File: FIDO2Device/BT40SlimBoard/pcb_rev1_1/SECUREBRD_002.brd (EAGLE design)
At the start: 30 x 30 mm, 36 parts, among them CN1 USB4105-GF-A, CN3 IF_6PIN, SW1 SKRPACE010, SW2 SKTADAE010, U1 BT40, U2 ADP122ACPZ-3.3-R7, U3 RV-3028-C7

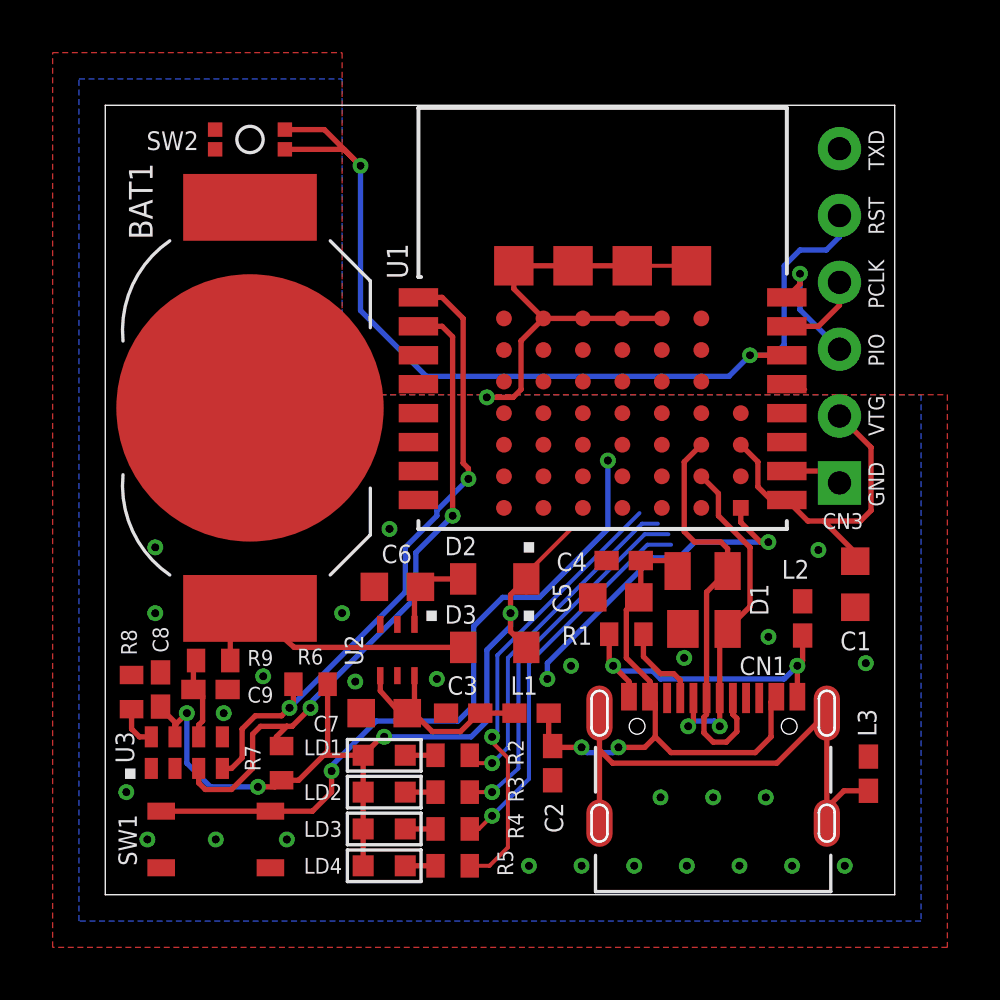
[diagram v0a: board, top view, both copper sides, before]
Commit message: 配線レイアウトを修正
・基板右側の配線レイアウトを変更
（配線が基板の端を通らないよう修正）
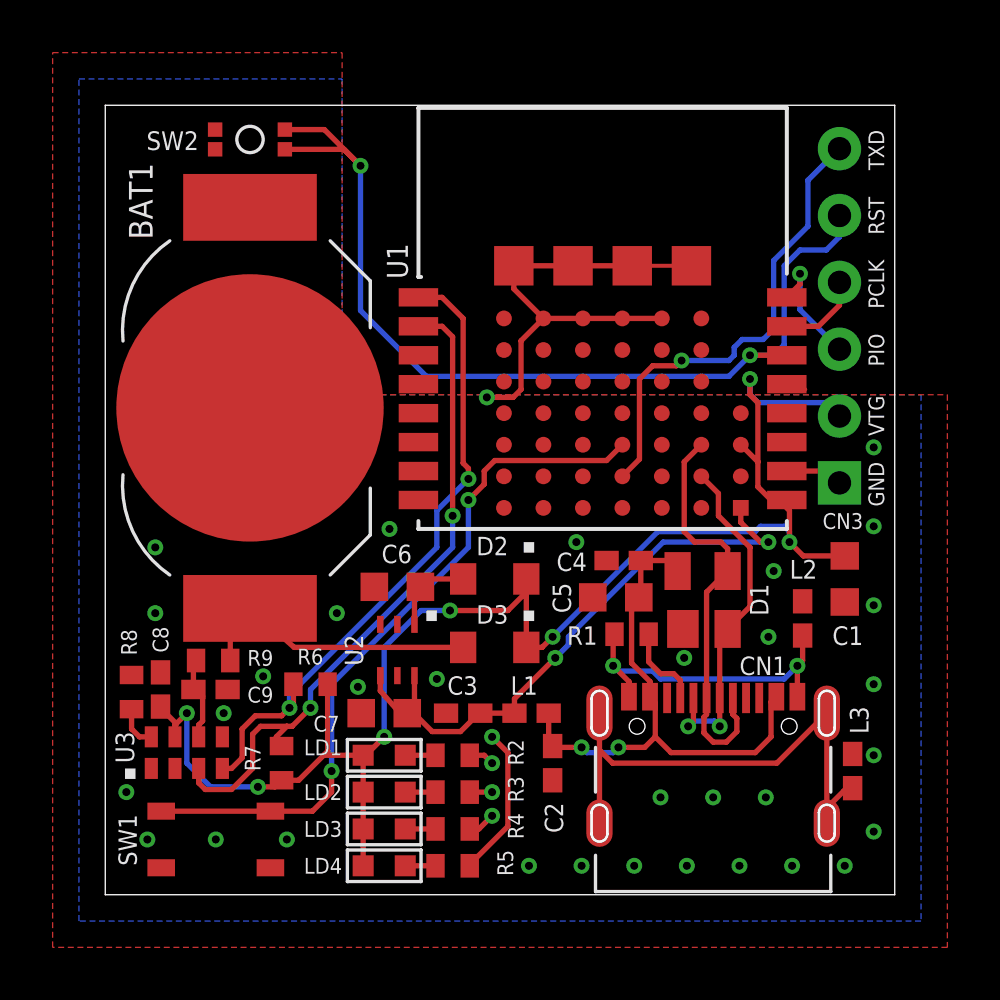
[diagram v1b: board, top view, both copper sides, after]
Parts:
- moved L3 0.61 mm to (28.4, 4.70)
- moved C1 0.45 mm to (28.1, 12.0)
- moved R1 0.20 mm to (20.0, 9.90)
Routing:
- net TXD: track 0.00 -> 17.9 mm, vias 0 -> 1
- net LED3: track 15.4 -> 1.79 mm
- net LED2: track 14.0 -> 0.85 mm
- net VDD_NRF: track 48.0 -> 60.1 mm, vias 4 -> 7
- net LED1: track 13.0 -> 0.97 mm
- net LED4: track 17.0 -> 5.75 mm
- net VBUS_NRF: track 20.9 -> 22.9 mm
- net SW1: track 26.4 -> 27.0 mm
- net FG: track 19.9 -> 19.3 mm
- net 0V: vias 28 -> 33

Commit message: 配線レイアウトを修正
・LED1〜4の配線レイアウトを変更
（ピン割り当ての変更無し）
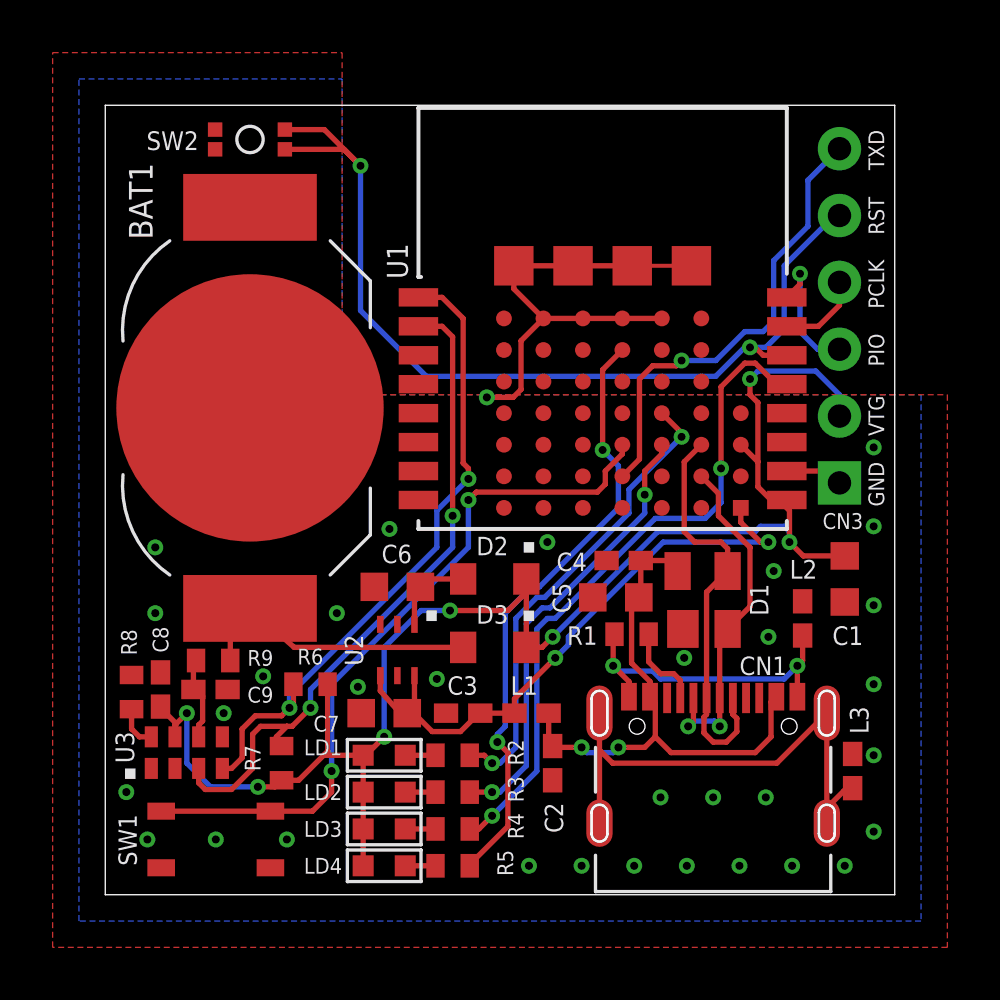
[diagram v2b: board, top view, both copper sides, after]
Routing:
- net LED3: track 1.79 -> 25.5 mm, vias 1 -> 2
- net LED4: track 5.75 -> 23.0 mm, vias 1 -> 2
- net LED1: track 0.97 -> 17.9 mm, vias 1 -> 2
- net LED2: track 0.85 -> 17.1 mm, vias 1 -> 2
- net RESET: track 37.5 -> 36.8 mm

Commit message: 配線レイアウトを修正
・裏面べたGNDパターンを改善
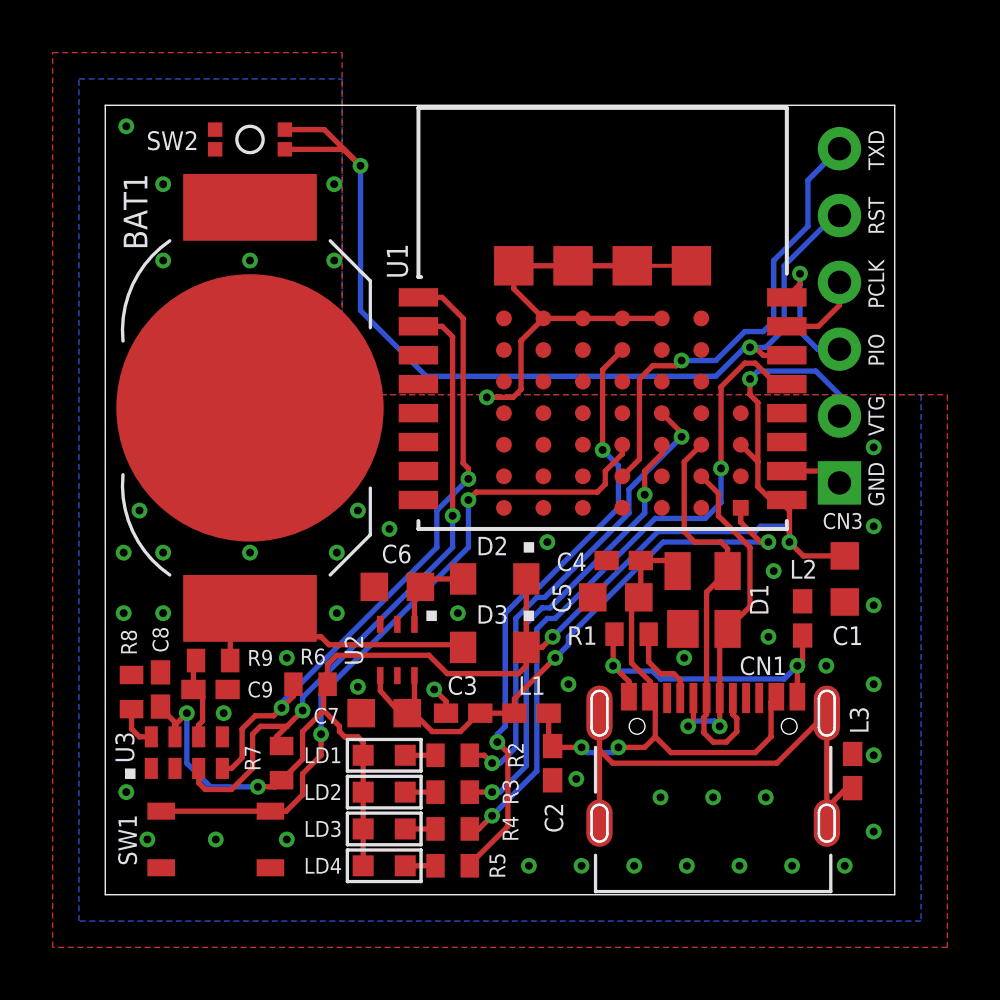
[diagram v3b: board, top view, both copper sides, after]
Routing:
- net 0V: track 20.4 -> 21.5 mm, vias 33 -> 49
- net SW1: track 27.2 -> 26.7 mm
- net VDD_NRF: track 60.5 -> 60.1 mm, vias 7 -> 5
